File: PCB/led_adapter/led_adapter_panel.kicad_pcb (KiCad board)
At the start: 2 copper layers, 47.2 x 42.4 mm, 33 parts, among them J1 SK6812MINI-E-012_mate, J10 SK6812MINI-E-012_mate, J11 SK6812MINI-E-012_mate, J12 SK6812MINI-E-012_mate, J13 SK6812MINI-E-012_mate, J14 SK6812MINI-E-012_mate, J15 SK6812MINI-E-012_mate, J16 SK6812MINI-E-012_mate, J2 SK6812MINI-E-012_mate, J3 SK6812MINI-E-012_mate, J4 SK6812MINI-E-012_mate, J5 SK6812MINI-E-012_mate, J6 SK6812MINI-E-012_mate, J7 SK6812MINI-E-012_mate, J8 SK6812MINI-E-012_mate, J9 SK6812MINI-E-012_mate

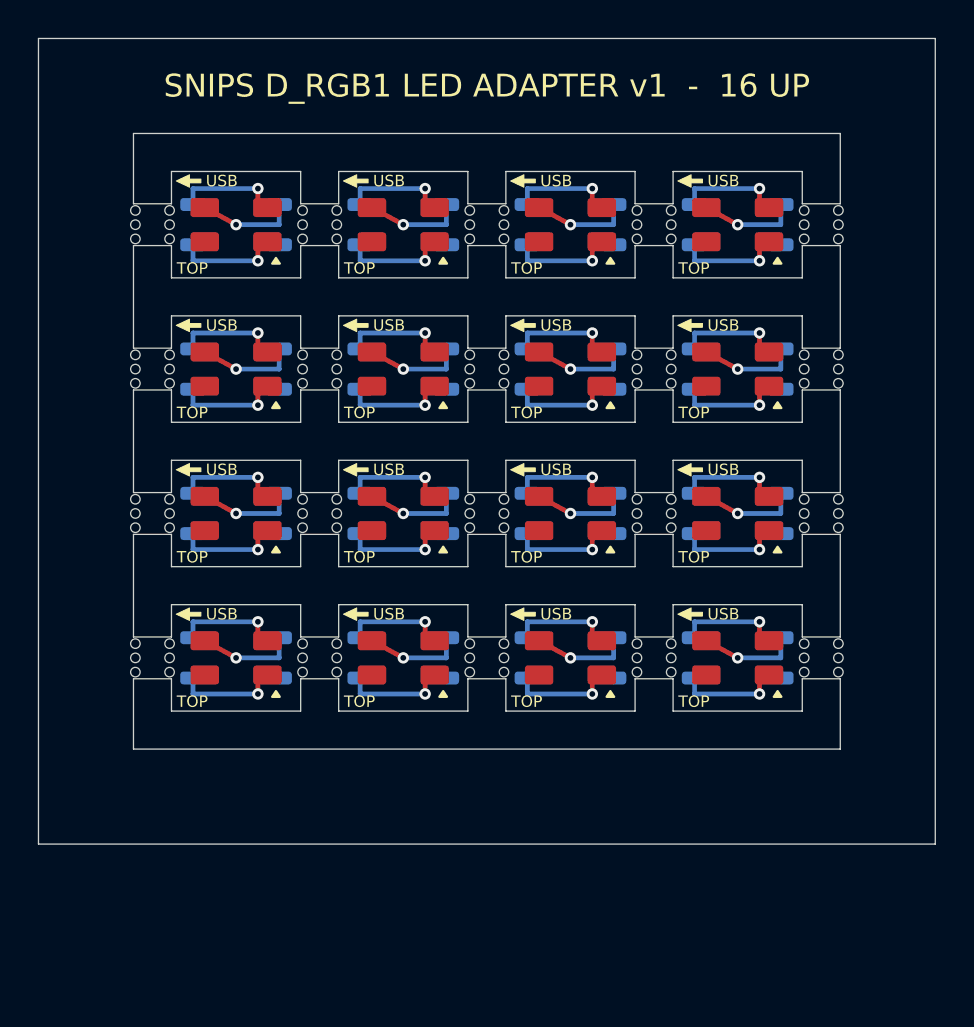
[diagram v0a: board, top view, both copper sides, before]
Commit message: Panel 20 adapters (4x5) to cover Alex's 10 boards
Alex has 10 rev-1 boards, not 5, so 20 boards need the adapter. Panel is
now 4 columns x 5 rows, 47.2 x 50.0 mm. DRC still 0/0; drill counts 60 PTH
(20 x 3 vias) and 150 NPTH mouse bites (25 tabs x 6).

Co-Authored-By: Claude Opus 5.5 <noreply@anthropic.com>
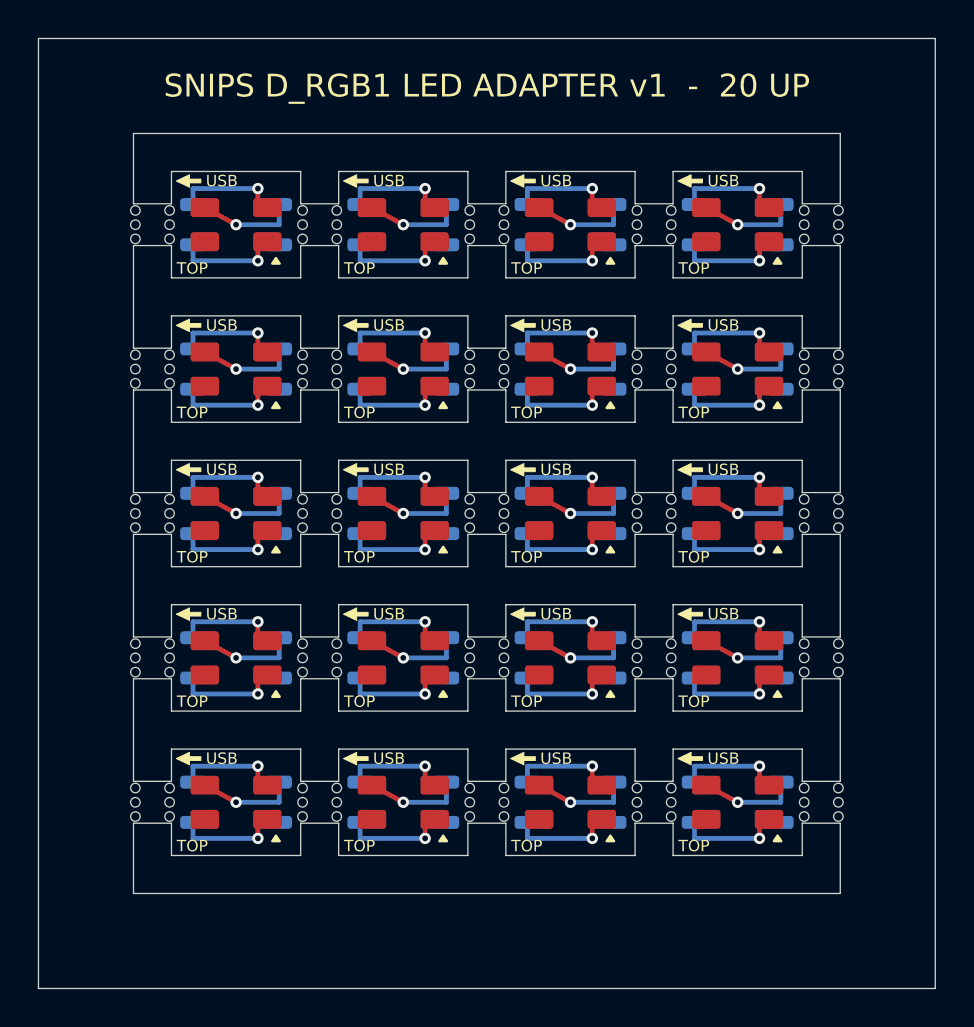
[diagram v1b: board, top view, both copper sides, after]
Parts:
- added D17: SK6812MINI-HS-012, SK6812MINI-HS-012, F.Cu at (110.4, 140.2)
- added D18: SK6812MINI-HS-012, SK6812MINI-HS-012, F.Cu at (119.2, 140.2)
- added D19: SK6812MINI-HS-012, SK6812MINI-HS-012, F.Cu at (128.0, 140.2)
- added D20: SK6812MINI-HS-012, SK6812MINI-HS-012, F.Cu at (136.8, 140.2)
- added J17: SK6812MINI-E-012_mate, SK6812MINI-E-012_mate, B.Cu at (110.4, 140.2)
- added J18: SK6812MINI-E-012_mate, SK6812MINI-E-012_mate, B.Cu at (119.2, 140.2)
- added J19: SK6812MINI-E-012_mate, SK6812MINI-E-012_mate, B.Cu at (128.0, 140.2)
- added J20: SK6812MINI-E-012_mate, SK6812MINI-E-012_mate, B.Cu at (136.8, 140.2)
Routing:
- net /A19/DIN: track 0.00 -> 5.26 mm, vias 0 -> 1
- net /A17/DIN: track 0.00 -> 5.26 mm, vias 0 -> 1
- net /A20/DIN: track 0.00 -> 5.26 mm, vias 0 -> 1
- net /A18/DIN: track 0.00 -> 5.26 mm, vias 0 -> 1
- net /A19/GND: track 0.00 -> 5.26 mm, vias 0 -> 1
- net /A17/GND: track 0.00 -> 5.26 mm, vias 0 -> 1
- net /A20/GND: track 0.00 -> 5.26 mm, vias 0 -> 1
- net /A18/GND: track 0.00 -> 5.26 mm, vias 0 -> 1
- net /A19/3V3: track 0.00 -> 5.21 mm, vias 0 -> 1
- net /A18/3V3: track 0.00 -> 5.21 mm, vias 0 -> 1
- net /A17/3V3: track 0.00 -> 5.21 mm, vias 0 -> 1
- net /A20/3V3: track 0.00 -> 5.21 mm, vias 0 -> 1
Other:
- board size 47.2 x 42.4 mm -> 47.2 x 50 mm
- board text added: "SNIPS D_RGB1 LED ADAPTER v1 - 20 UP"
- board text removed: "SNIPS D_RGB1 LED ADAPTER v1 - 16 UP"

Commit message: Go back to a 4x4 panel of 16 adapters
The fab minimum of 5 panels gives 80 adapters, plenty for the 20 rev-1
boards, so the 4x5 panel isn't needed. DRC 0/0; drill counts 48 PTH and
120 NPTH.

Co-Authored-By: Claude Opus 5.5 <noreply@anthropic.com>
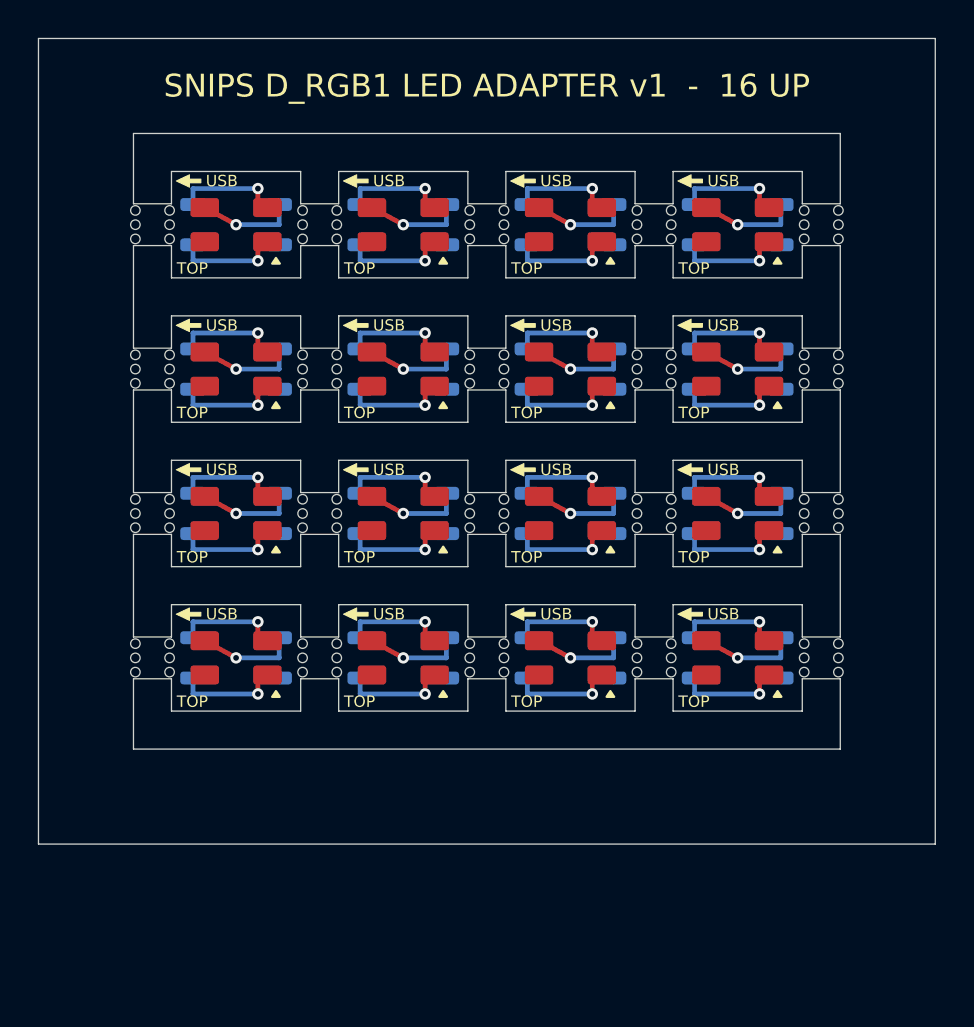
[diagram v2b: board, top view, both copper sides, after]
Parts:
- removed D17, D18, D19, D20: SK6812MINI-HS-012, SK6812MINI-HS-012
- removed J17, J18, J19, J20: SK6812MINI-E-012_mate, SK6812MINI-E-012_mate
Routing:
- net /A19/DIN: track 5.26 -> 0.00 mm, vias 1 -> 0
- net /A17/DIN: track 5.26 -> 0.00 mm, vias 1 -> 0
- net /A20/DIN: track 5.26 -> 0.00 mm, vias 1 -> 0
- net /A18/DIN: track 5.26 -> 0.00 mm, vias 1 -> 0
- net /A19/GND: track 5.26 -> 0.00 mm, vias 1 -> 0
- net /A17/GND: track 5.26 -> 0.00 mm, vias 1 -> 0
- net /A20/GND: track 5.26 -> 0.00 mm, vias 1 -> 0
- net /A18/GND: track 5.26 -> 0.00 mm, vias 1 -> 0
- net /A19/3V3: track 5.21 -> 0.00 mm, vias 1 -> 0
- net /A18/3V3: track 5.21 -> 0.00 mm, vias 1 -> 0
- net /A17/3V3: track 5.21 -> 0.00 mm, vias 1 -> 0
- net /A20/3V3: track 5.21 -> 0.00 mm, vias 1 -> 0
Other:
- board size 47.2 x 50 mm -> 47.2 x 42.4 mm
- board text added: "SNIPS D_RGB1 LED ADAPTER v1 - 16 UP"
- board text removed: "SNIPS D_RGB1 LED ADAPTER v1 - 20 UP"
